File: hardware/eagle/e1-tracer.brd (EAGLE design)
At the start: 100 x 75 mm, 114 parts, among them IC1 MCP1703T-1202E/CB, IC2 W25Q80DVSNIG, IC3 TLV70233DBVR, IC4 ASEM1-12.000MHZ-LC-T, J1 PASSTHROUGH, M1 MENTOR_12701001, M2 MENTOR_12701001, SW1 TACTSW-TL3340, T1 BC847C, T2 BC847C, U1 ICE40UP5K-SG48I, U2 IP4234CZ6, U3 IP4234CZ6, U4 IDT82V2081, U5 IDT82V2081, U6 2.048 Mhz, U7 1.544 MHz, X1 MINI-USB-SHIELD-UX60-MB-5ST, X2 JACK2.5_SJ-2523

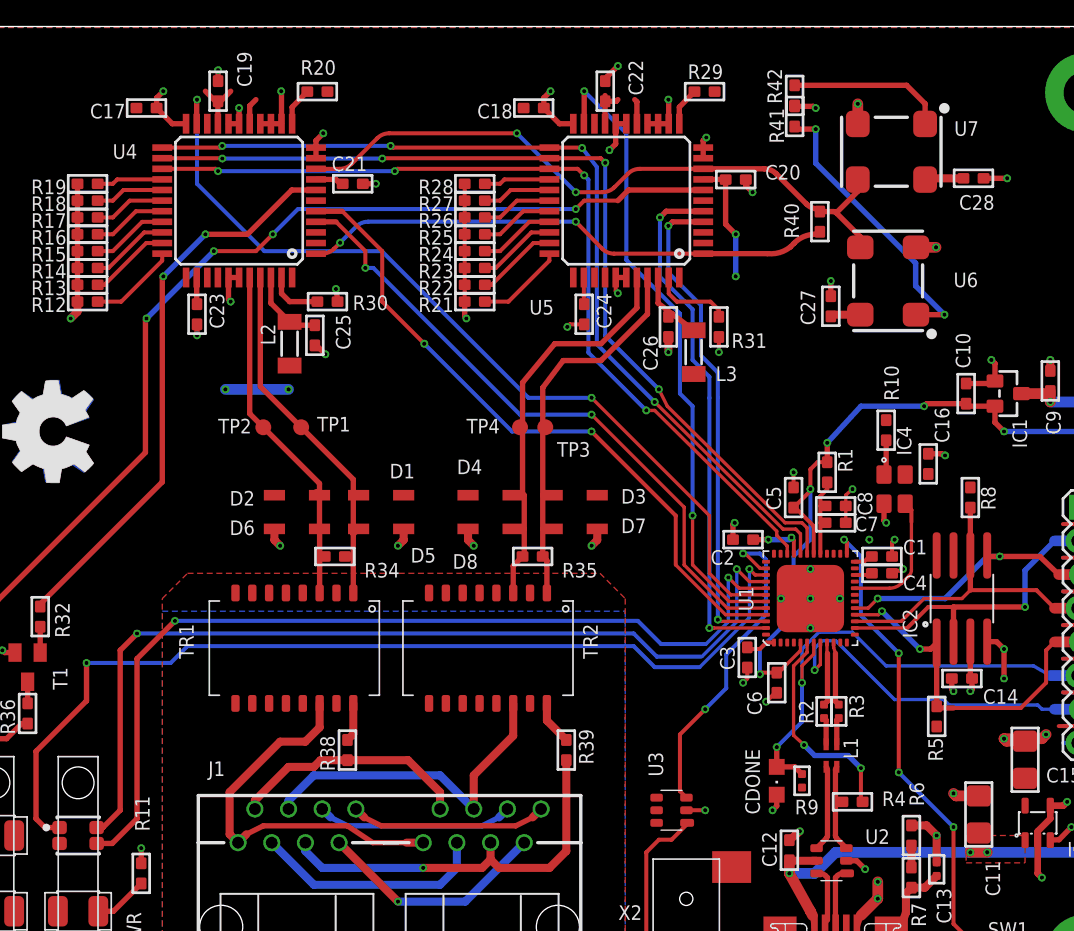
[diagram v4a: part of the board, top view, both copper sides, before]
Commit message: e1-tracer: improve power bypassing on LIU's VDDT and VDDA
...by placing 2x 22u per LIU (instead of 68u DNP), shrinking packages
from 1206 to 0805
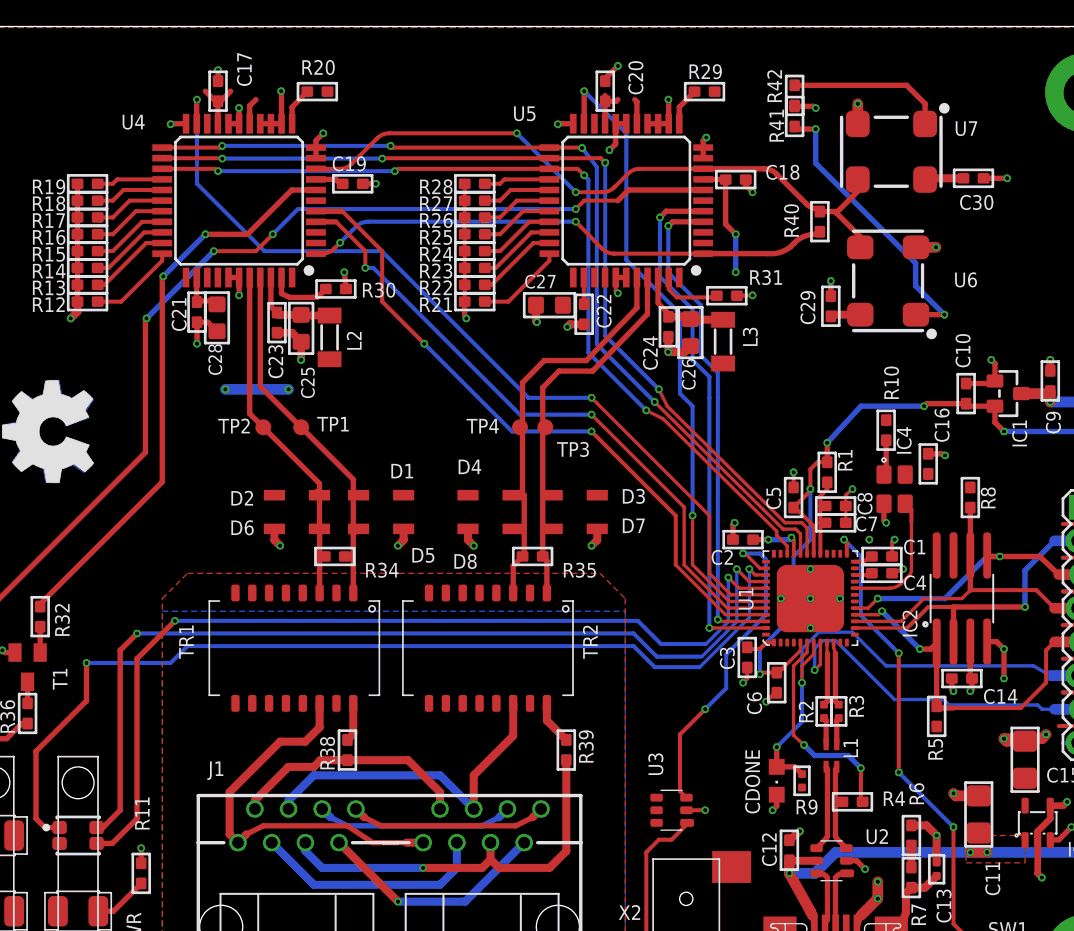
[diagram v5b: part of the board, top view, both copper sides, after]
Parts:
- added C29, C30: 100n, rc-sysmocom:_0603
- C17, C18: value 68µ DNP -> 100n
- C25, C26, C27, C28: value 100n -> 22u; device rc-sysmocom:_0603 -> rc-sysmocom:_0805
- moved C28 58.0 mm to (29.5, 53.0), turned to 90 degrees
- moved C27 21.2 mm to (54.6, 54.0), turned to 0 degrees
- moved C22 16.9 mm to (57.2, 53.3), turned to 270 degrees
- moved C18 16.2 mm to (68.7, 63.5), turned to 0 degrees
- moved C21 15.2 mm to (28.0, 53.5), turned to 270 degrees
- moved C19 12.3 mm to (39.8, 63.1), turned to 0 degrees
- moved C20 11.9 mm to (58.8, 70.1), turned to 90 degrees
- moved C24 6.42 mm to (63.6, 52.3)
- moved C23 6.07 mm to (34.1, 52.7)
- moved C17 5.54 mm to (29.6, 70.1), turned to 90 degrees
- moved L2 3.05 mm to (38.0, 51.5)
- moved R31 2.43 mm to (68.0, 54.7), turned to 180 degrees
- moved L3 2.36 mm to (67.7, 51.2)
- moved C26 1.72 mm to (65.2, 51.9), turned to 90 degrees
- moved C25 1.16 mm to (35.9, 52.2), turned to 90 degrees
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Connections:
- net GND: now also C17.2, C18.2, C25.1, C26.1, C29.1, C30.1; no longer C17.1, C18.1, C25.2, C26.2
- net N$23: now also C23.1, C25.2; no longer C25.1
- net N$3: now also C24.1, C26.2; no longer C26.1
- net VCC_3V3: now also C17.1, C18.1, C29.2, C30.2; no longer C17.2, C18.2, C23.1, C24.1
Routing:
- net GND: track 155.9 -> 157.8 mm, vias 72 -> 73
- net N$3: track 5.67 -> 7.55 mm
- net VCC_3V3: track 68.8 -> 70.2 mm
- net N$1: track 6.02 -> 4.79 mm
- net N$23: track 5.94 -> 6.90 mm
- net N$4: track 4.17 -> 4.86 mm

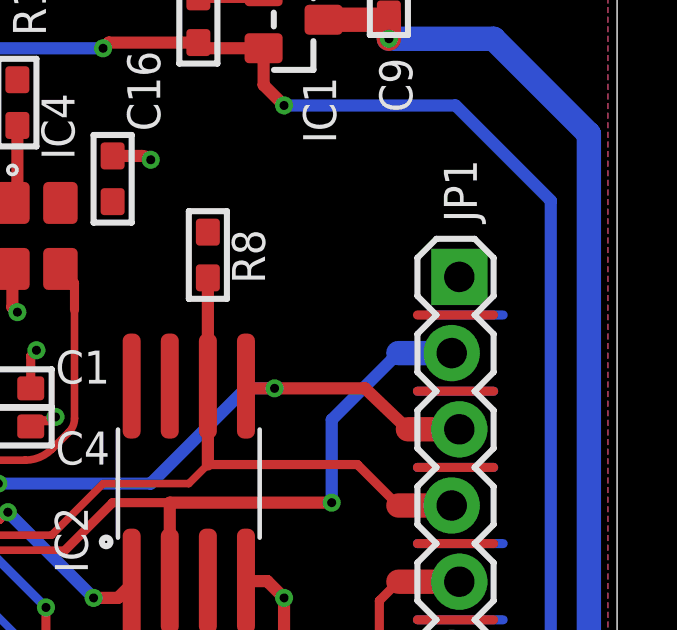
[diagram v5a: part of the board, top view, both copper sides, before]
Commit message: e1-tracer: add a generic 0603 blue LED type w/ Vf=2.8V
designating LTST-C193TBKT-5A for now
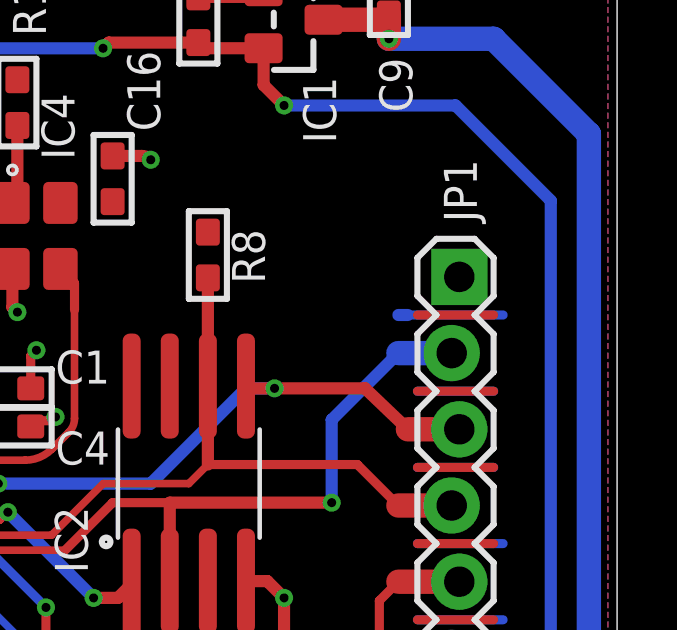
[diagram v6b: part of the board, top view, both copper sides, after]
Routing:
- net GND: track 157.8 -> 158.8 mm
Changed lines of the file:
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@@
 </element>
 <element name="CDONE" library="led" package="CHIPLED_0805" value="BLUE" x="71.755" y="18.0975" smashed="yes" rot="R180">
-<attribute name="LINK" value="UNKNOWN LINK" x="71.755" y="18.0975" size="1.778" layer="27" rot="R180" display="off"/>
+<attribute name="LINK" value="https://www.digikey.de/product-detail/de/lite-on-inc/LTST-C193TBKT-5A/160-1827-1-ND" x="71.755" y="18.0975" size="1.778" layer="27" rot="R180" display="off"/>
 <attribute name="SOURCEPARTNUMBER" value="UNKNOWN SOURCE PART NUMBER" x="71.755" y="18.0975" size="1.778" layer="27" rot="R180" display="off"/>
 <attribute name="MANUFACTURERPARTNUMBER" value="UNKNOWN MANUFACTURER PART NUMBER" x="71.755" y="18.0975" size="1.778" layer="27" rot="R180" display="off"/>
@@
 </elements>
 <signals>
-<signal name="GND">
+<signal name="GND" class="1">
 <contactref element="U1" pad="EXP"/>
 <contactref element="C3" pad="1"/>
@@
 <wire x1="93.345" y1="27.305" x2="96.2025" y2="27.305" width="0.3048" layer="16"/>
 <wire x1="93.345" y1="24.765" x2="96.2025" y2="24.765" width="0.3048" layer="16"/>
-<wire x1="93.6625" y1="37.465" x2="96.2025" y2="37.465" width="0.3048" layer="16"/>
+<wire x1="93.0275" y1="37.465" x2="96.2025" y2="37.465" width="0.3048" layer="16"/>
 <wire x1="68.20285" y1="1.89125" x2="68.24875" y2="1.25625" width="0.4064" layer="1"/>
 <wire x1="68.24875" y1="1.25625" x2="68.2625" y2="4.1275" width="0.4064" layer="1"/>
@@
 <wire x1="55.2825" y1="67.665" x2="55.245" y2="67.6275" width="0.4064" layer="1"/>
 <via x="55.245" y="67.6275" extent="1-16" drill="0.3048"/>
+<wire x1="92.71" y1="37.465" x2="93.0275" y2="37.465" width="0.4064" layer="16"/>
 </signal>
 <signal name="VCC_3V3" class="1">

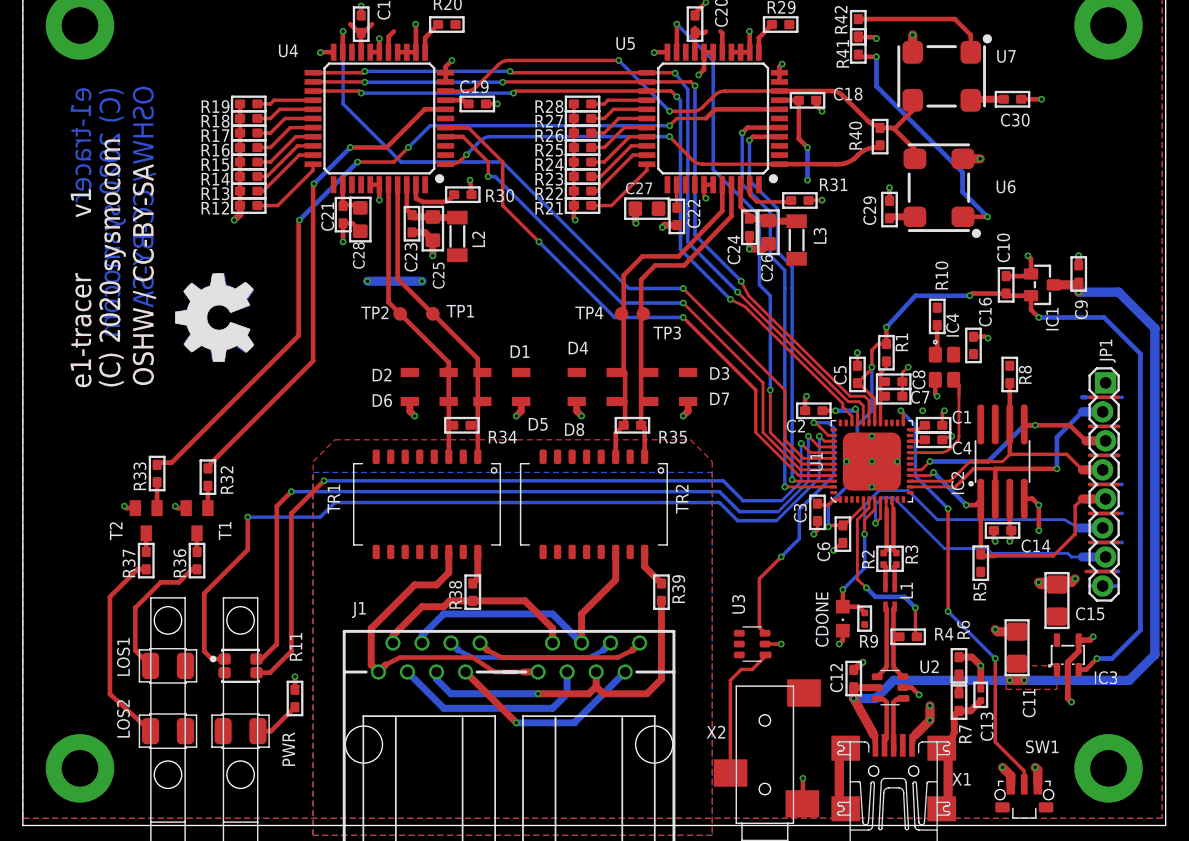
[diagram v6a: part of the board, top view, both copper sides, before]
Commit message: e1-tracer: have more clearance of VBUS trace on PCB edge
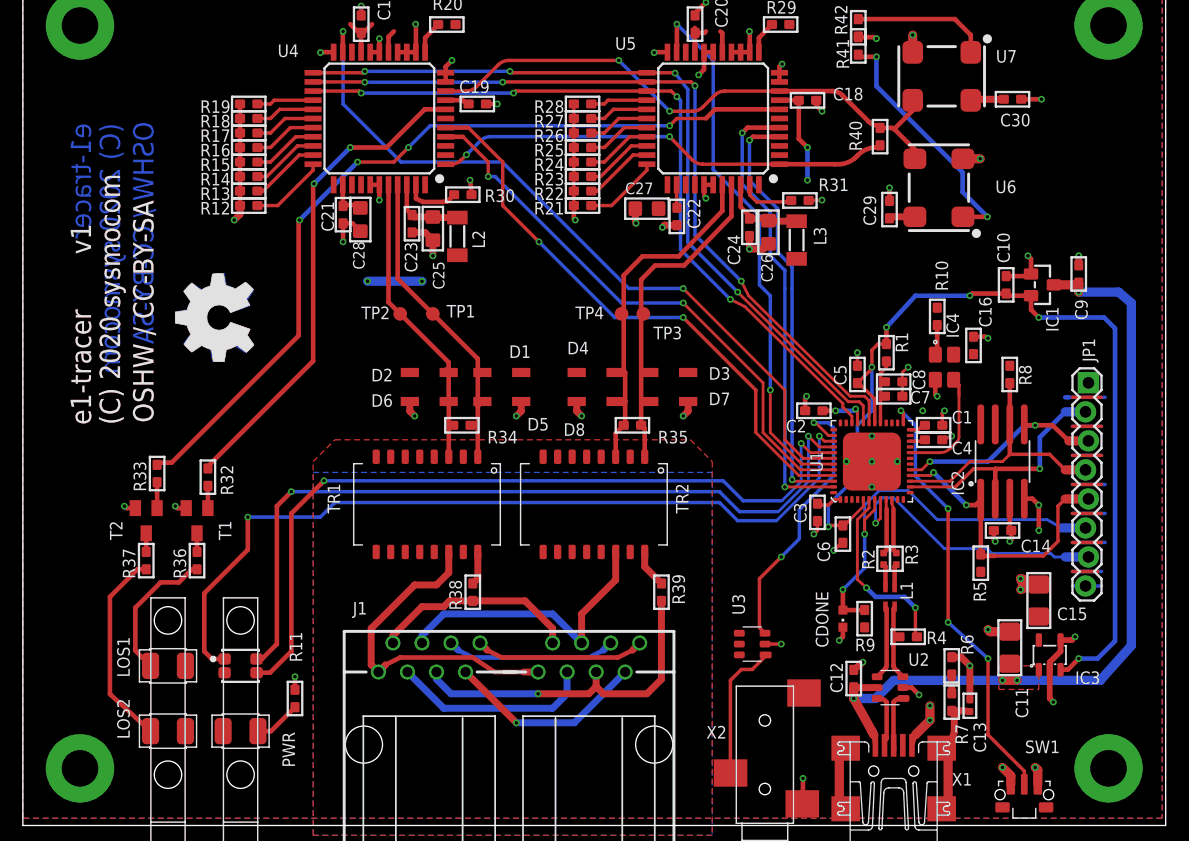
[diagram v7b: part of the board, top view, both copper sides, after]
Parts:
- CDONE: device led:CHIPLED_0805 -> led:CHIPLED_0603
- R9: device rc-sysmocom:_0402 -> rc-sysmocom:_0603
- moved C15 1.59 mm to (88.9, 19.7)
- moved IC3 1.59 mm to (89.9, 14.9)
- moved JP1 1.50 mm to (93.1, 38.7)
- moved C13 1.35 mm to (82.9, 10.5)
- moved C11 0.64 mm to (86.4, 15.6)
- moved R6 0.64 mm to (81.3, 14.0)
- moved R7 0.64 mm to (81.3, 10.8)
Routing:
- net VBUS: track 77.7 -> 74.5 mm
- net IOB_34A_SPI_SCK: track 24.6 -> 23.1 mm
- net IOB_33B_SPI_SI: track 20.2 -> 18.7 mm
- net IOB_32A_SPI_SO: track 23.8 -> 22.3 mm
- net !CRESET: track 26.4 -> 24.9 mm
- net CDONE: track 37.8 -> 36.4 mm
- net IOB_35B_SPI_SS: track 26.9 -> 25.8 mm
- net VCC_1V2: track 87.9 -> 86.9 mm
- net GND: track 158.8 -> 159.7 mm
- net N$61: track 12.8 -> 12.0 mm

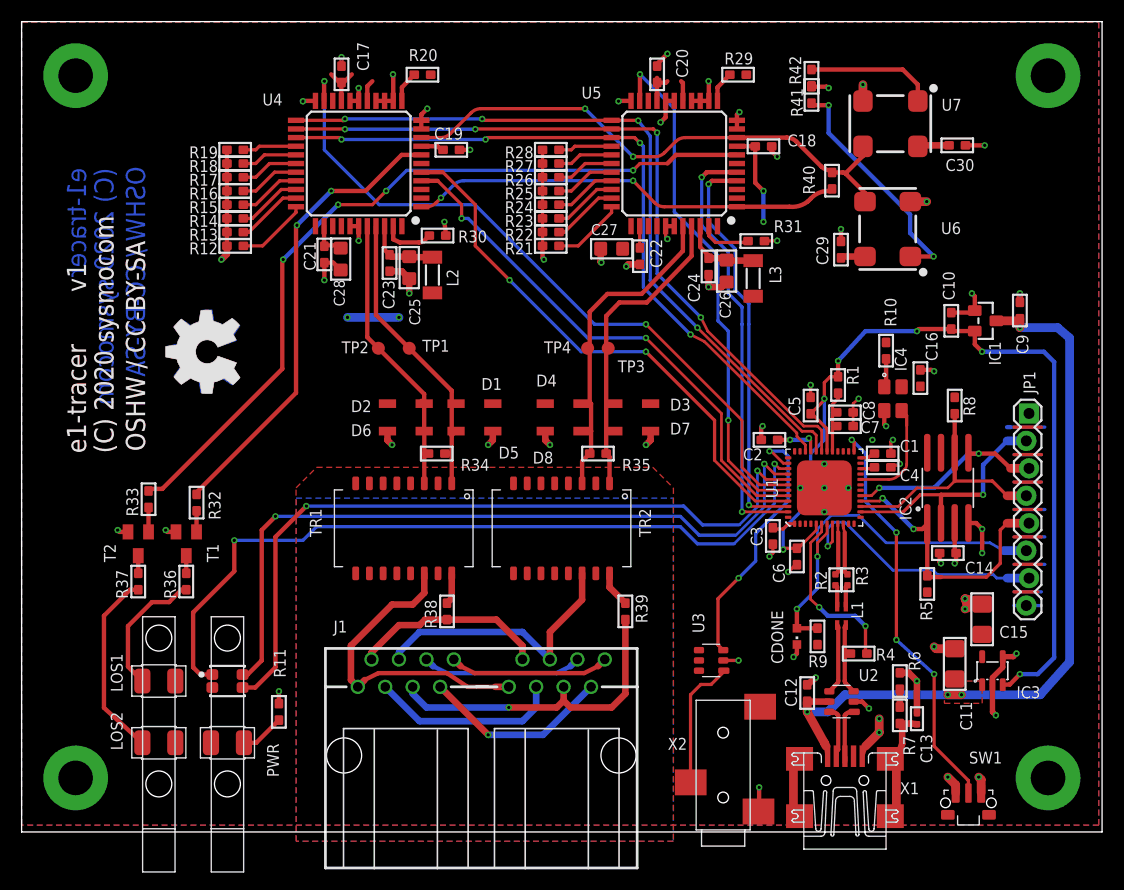
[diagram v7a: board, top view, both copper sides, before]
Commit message: e1-tracer: 4x 0R on R and B LED color selection wires
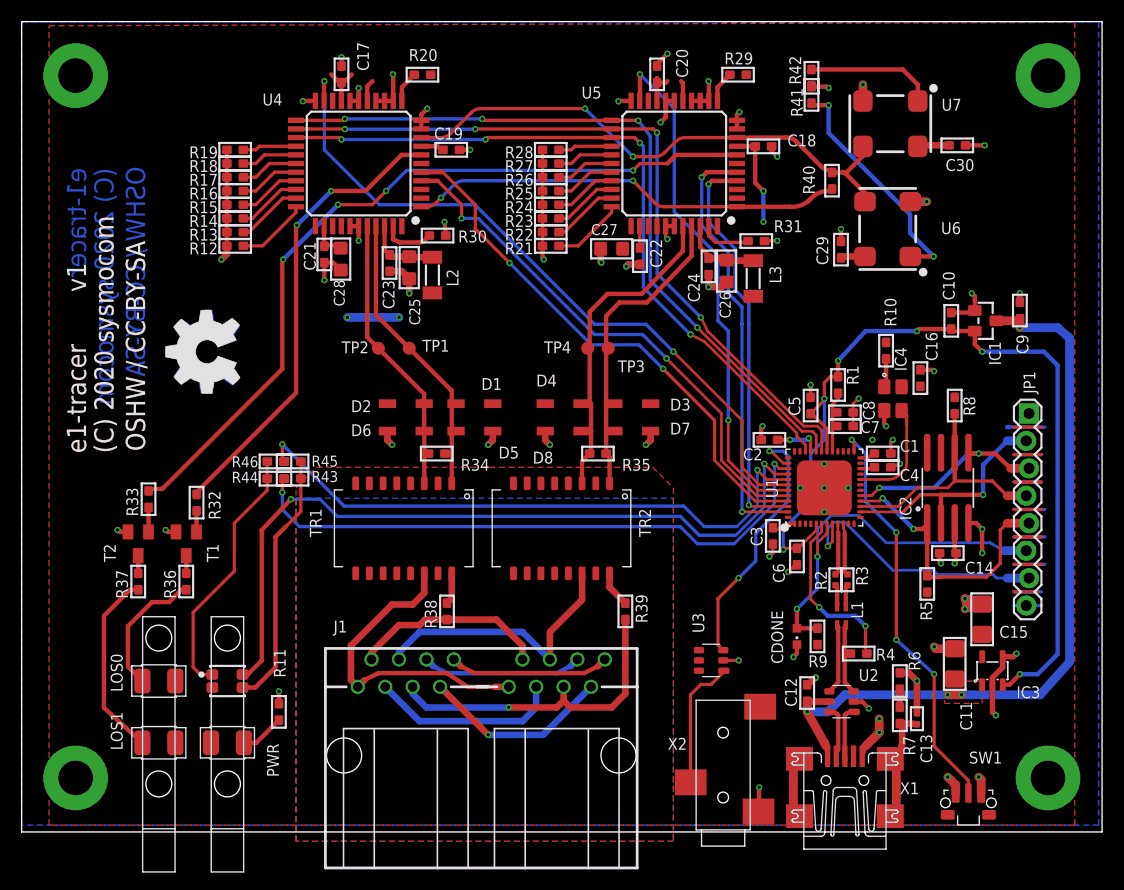
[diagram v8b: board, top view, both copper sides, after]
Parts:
- removed LOS2: LEDPLCC2-MIN-red, LED-PLCC2:PLCC2-MIN
- added LOS0: LEDPLCC2-MIN-red, LED-PLCC2:PLCC2-MIN
- added R43, R44, R45, R46: DNP, rc-sysmocom:_0603
- moved LOS1 5.71 mm to (12.7, 8.26)
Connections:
- new net N$45: R45.2, R46.1, U1.41
- new net N$46: LED1.1, R44.2, R46.2
- net N$27: now also LOS0.K; no longer LOS1.K
- net N$37: now also LOS1.K; no longer LOS2.K
- net N$63: now also R43.2, R44.1; no longer LED1.1
- net N$65: now also R43.1, R45.1; no longer U1.41
- net VCC_3V3: now also LOS0.A; no longer LOS2.A
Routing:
- net N$45: track 0.00 -> 56.2 mm, vias 0 -> 2
- net N$65: track 69.6 -> 23.8 mm, vias 2 -> 0
- net N$46: track 0.00 -> 23.9 mm
- net N$63: track 73.2 -> 56.5 mm
- net N$64: track 69.8 -> 71.2 mm
- net IO_B1: track 51.0 -> 50.0 mm
